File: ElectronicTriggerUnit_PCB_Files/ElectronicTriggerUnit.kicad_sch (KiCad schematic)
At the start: 51 parts, among them IC1 MCP1407-E_SN, IC2 ATTINY814-SSF, J2 Conn_01x05, J4 Conn_01x04, M1 Motor_DC, Q1 LC191PTDT, Q2 LKPT30102B-A01, Q3 78-SQRS140ELP, Q4 LC191PTDT, U1 Gnd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

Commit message: changed some parts
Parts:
- removed D4: D, Diode_SMD:D_0603_1608Metric, symbol Device:D
- added IC3: BU4S584G2-TR, SamacSys:SOT95P280X125-5N, symbol SamacSys:BU4S584G2-TR
- Q3: value 78-SQRS140ELP -> SIR500DP-T1-RE3
- R4: footprint Resistor_SMD:R_0603_1608Metric -> Resistor_SMD:R_1206_3216Metric
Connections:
- net +3.3V: now also IC3.5 (VDD)
- net GND: now also IC1.7 (OUT_2), IC1.8 (VDD_2), IC3.3 (VSS)
- net trigger_Out: now also IC3.4 (Y); no longer C11.2, R13.2
- new net: C11.2, IC3.2 (A), R13.2
- no-connect marks 9 -> 7
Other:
- note removed: "P=I^2 * R P=150 *150 * 0.0006 P=13.5 W Temp= 4.2 * 13.5 + 25 = 81.7 degC pulse 100ms Pcont = 20 * 20 * 0.0006 = 0.24 W Temp cont = 42 * 0.24 + 25 = 35.08 degC continous"
- note removed: "R4Min= (VCC-GND)/ID(IC1) = 12-0/1.3=9.23 -> min 10R"
- note removed: "V=I * R I= 12/10 = 1.2 A TOpen = charge/I = 294 nC / 1.2 = 245 ns PR4 = 1.2*1.2*10=14.4W ptr 245 ns"
- moved on the sheet: C1, C11, C12, D2, IC1, LED2, M1, Q3, Q4, R13, R14, R4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

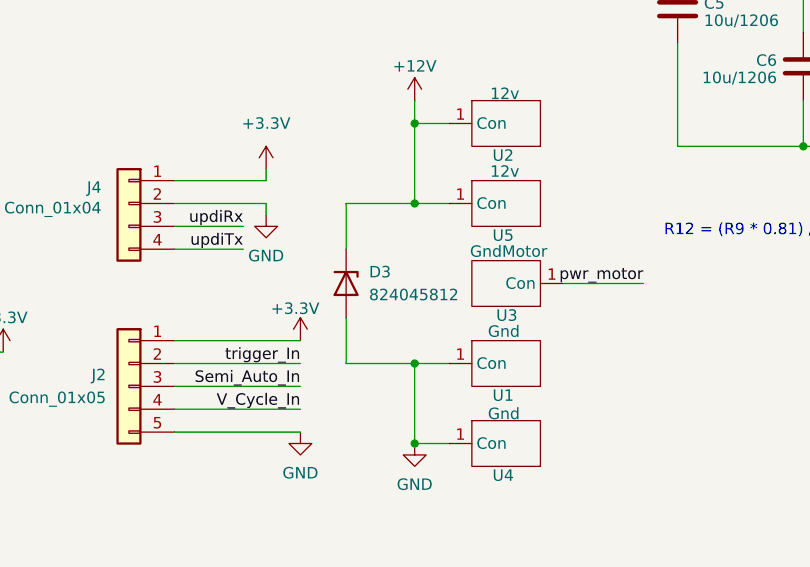
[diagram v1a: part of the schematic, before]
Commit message: redid ground plane and trace spacing
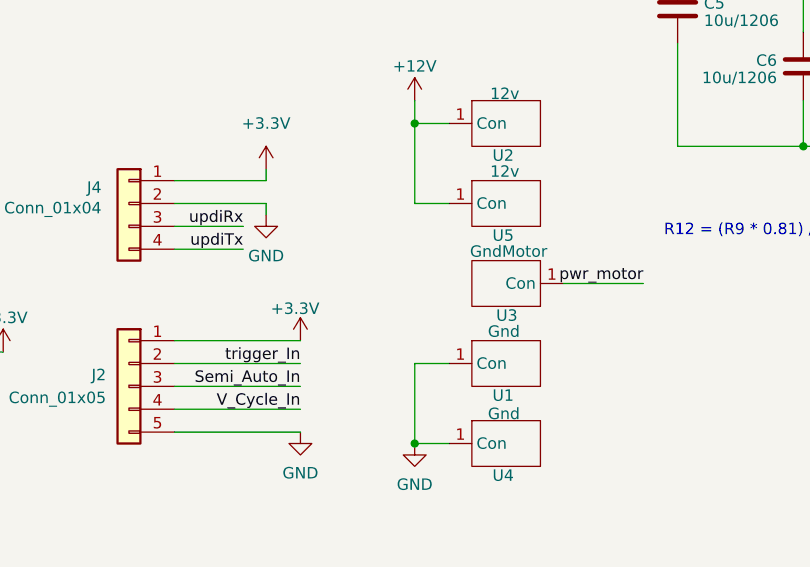
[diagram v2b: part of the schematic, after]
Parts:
- removed D3: 824045812, SamacSys:TVS_DIODE, symbol Diode:ESD5Zxx
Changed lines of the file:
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@@
 	)
 	(junction
-		(at 149.86 182.88)
-		(diameter 0)
-		(color 0 0 0 0)
-	)
-	(junction
 		(at 259.08 106.68)
 		(diameter 0)
@@
 	)
 	(junction
-		(at 149.86 165.1)
-		(diameter 0)
-		(color 0 0 0 0)
-	)
-	(junction
 		(at 40.64 88.9)
 		(diameter 0)
@@
 	(wire
 		(pts
-			(xy 142.24 170.18) (xy 142.24 165.1)
-		)
-		(stroke
-			(width 0)
-			(type default)
-		)
-	)
-	(wire
-		(pts
 			(xy 102.87 54.61) (xy 121.92 54.61)
 		)
@@
 	(wire
 		(pts
-			(xy 142.24 177.8) (xy 142.24 182.88)
-		)
-		(stroke
-			(width 0)
-			(type default)
-		)
-	)
-	(wire
-		(pts
 			(xy 198.12 35.56) (xy 198.12 33.02)
 		)
@@
 	(wire
 		(pts
-			(xy 142.24 165.1) (xy 149.86 165.1)
-		)
-		(stroke
-			(width 0)
-			(type default)
-		)
-	)
-	(wire
-		(pts
 			(xy 196.85 137.16) (xy 196.85 138.43)
 		)
@@
 	(wire
 		(pts
-			(xy 142.24 182.88) (xy 149.86 182.88)
-		)
-		(stroke
-			(width 0)
-			(type default)
-		)
-	)
-	(wire
-		(pts
 			(xy 255.27 158.75) (xy 262.89 158.75)
 		)
@@
 					(unit 1)
 				)
-			)
-		)
-	)
-	(symbol
-		(lib_id "Diode:ESD5Zxx")
-		(at 142.24 173.99 270)
-		(unit 1)
-		(exclude_from_sim no)
-		(in_bom yes)
-		(on_board yes)
-		(dnp no)
-		(property "Reference" "D3"
-			(at 144.78 172.7199 90)
-			(effects
-				(font
-					(size 1.27 1.27)
-				)
-				(justify left)
-			)
-		)
-		(property "Value" "824045812"
-			(at 144.78 175.2599 90)
-			(effects
-				(font
-					(size 1.27 1.27)
-				)
-				(justify left)
-			)
-		)
-		(property "Footprint" "SamacSys:TVS_DIODE"
-			(at 137.795 173.99 0)
-			(effects
-				(font
-					(size 1.27 1.27)
-				)
-				(hide yes)
-			)
-		)
-		(property "Datasheet" "https://www.we-online.com/components/products/datasheet/824045812.pdf"
-			(at 142.24 173.99 0)
-			(effects
-				(font
-					(size 1.27 1.27)
-				)
-				(hide yes)
-			)
-		)
-		(property "Description" "ESD Protection Diodes / TVS Diodes WE-TVS DFN1610-2L 12V 440pF 1Channel"
-			(at 142.24 173.99 0)
-			(effects
-				(font
-					(size 1.27 1.27)
-				)
-				(hide yes)
-			)
-		)
-		(pin "1"
-		)
-		(pin "2"
-		)
-		(instances
-			(project ""
-				(path "/006bc43b-d3a8-4a38-a8dc-5a24da3f9b4d"
-					(reference "D3")
-					(unit 1)
-				)
